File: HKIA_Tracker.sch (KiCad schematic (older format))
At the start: 34 parts

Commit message: sch done
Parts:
- added C? (x5): 10uF, Capacitor_SMD:C_0805_2012Metric, symbol Device:C
- added C? (x6): 100nF, Capacitor_SMD:C_0805_2012Metric, symbol Device:C
- added C?: 10pF, Capacitor_SMD:C_0603_1608Metric, symbol Device:C
- added C?: 150pF, Capacitor_SMD:C_0603_1608Metric, symbol Device:C
- added C?: NC, Capacitor_SMD:C_0603_1608Metric, symbol Device:C
- added C?: 100pF, Capacitor_SMD:C_0603_1608Metric, symbol Device:C
- added C?: 1uF, Capacitor_SMD:C_0603_1608Metric, symbol Device:C
- added C?: 220nF, Capacitor_SMD:C_0603_1608Metric, symbol Device:C
- added C?: 4.7uF, Capacitor_SMD:C_0603_1608Metric, symbol Device:C
- added J?: SWD, Connector_PinHeader_1.27mm:PinHeader_2x05_P1.27mm_Vertical_SMD, symbol Connector_Generic:Conn_02x05_Odd_Even
- added J?: Conn_01x04, symbol Connector_Generic:Conn_01x04
- added L?: 10uH, Inductor_SMD:L_1210_3225Metric, symbol Device:L
- added L?: 22uH, Inductor_SMD:L_1210_3225Metric, symbol Device:L
- added R? (x3): 680k, Resistor_SMD:R_0603_1608Metric, symbol Device:R
- added R? (x3): 120k, Resistor_SMD:R_0603_1608Metric, symbol Device:R
- added R? (x6): 10K, Resistor_SMD:R_0603_1608Metric, symbol Device:R
- added SW? (x3): SW_Push, Button_Switch_SMD:SW_SPST_CK_KXT3, symbol Switch:SW_Push
- added U?: TPS62200DBV, Package_TO_SOT_SMD:SOT-23-5, symbol Regulator_Switching:TPS62200DBV
- added U?: E73-2G4M04S-52832, RF_Module:E73-2G4M04S, symbol RF_Module:E73-2G4M04S-52832
- added U?: ESP-12F, RF_Module:ESP-12E, symbol RF_Module:ESP-12F
- added U?: QMC5883L, Package_LGA:LGA-16_3x3mm_P0.5mm, symbol HKIA_Tracker_SYM:QMC5883L
- C?: value 10n -> 10nF
- C? (x2): value 100n -> 100nF
- R?: value 14K -> 56k; LCSC C103291 -> C304766
- R?: LCSC (none) -> C15402
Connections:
- net labels added: +3.3VP, +BATT, DRDY, ESP_EN, ESP_IO0, ESP_IO2, ESP_RX, ESP_TX, NRF_RX, NRF_TX, SCL, SDA, SWCLK, SWDIO, SWO, nRST
- wire segments 89 -> 216
- no-connect marks 2 -> 5
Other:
- note added: "ANT"
- moved on the sheet: C?, D?, F?, J?, JP?, L?, R?, U?

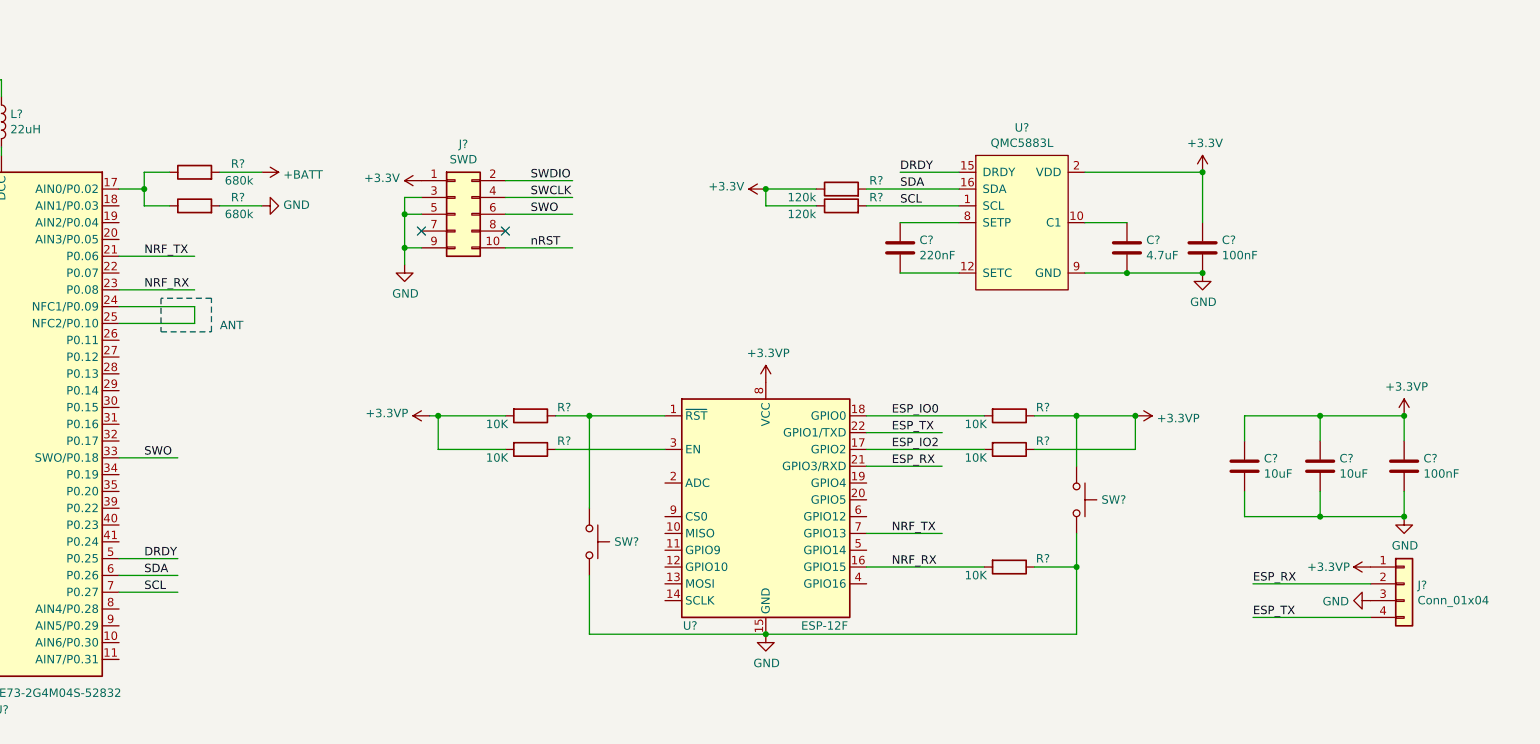
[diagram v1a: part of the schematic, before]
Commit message: add button and led
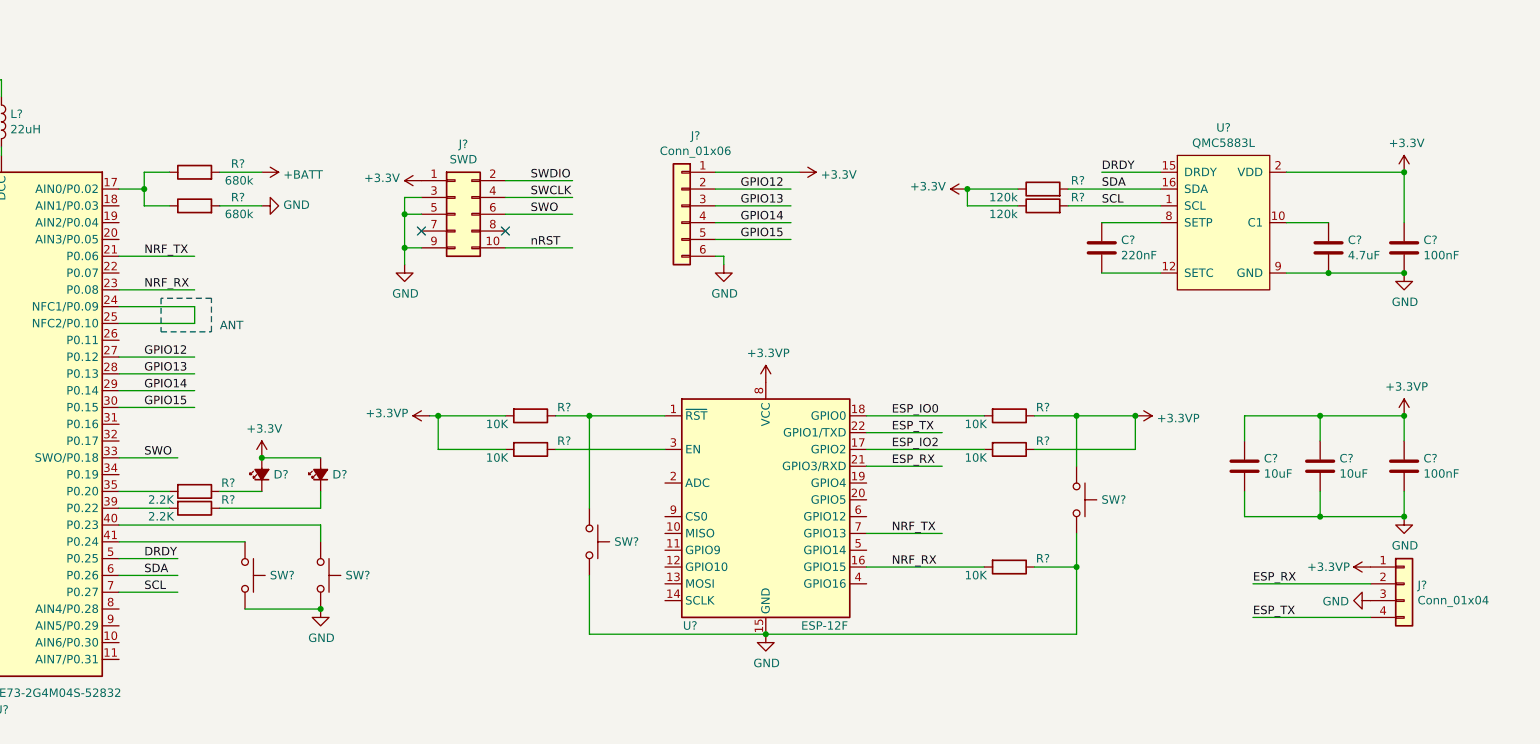
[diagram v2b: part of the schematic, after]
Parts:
- added D? (x2): LED_Small_ALT, Diode_SMD:D_0603_1608Metric, symbol Device:LED_Small_ALT
- added J?: Conn_01x06, Connector_PinHeader_2.54mm:PinHeader_1x06_P2.54mm_Vertical, symbol Connector_Generic:Conn_01x06
- added R? (x2): 2.2K, Resistor_SMD:R_0603_1608Metric, symbol Device:R
- added SW? (x2): SW_Push, Button_Switch_SMD:SW_SPST_CK_KXT3, symbol Switch:SW_Push
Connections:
- net labels added: GPIO12, GPIO13, GPIO14, GPIO15
- wire segments 216 -> 237
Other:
- moved on the sheet: C?, R?, U?

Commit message: fix issues
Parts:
- removed U?: QMC5883L, Package_LGA:LGA-16_3x3mm_P0.5mm, symbol HKIA_Tracker_SYM:QMC5883L
- added U5: QMC5883L, Package_LGA:LGA-16_3x3mm_P0.5mm, symbol HKIA_Tracker_SYM:QMC5883L
- gave numbers to parts that had none: 81
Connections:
- wire segments 237 -> 241
- no-connect marks 5 -> 28
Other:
- moved on the sheet: J4

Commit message: added power jumpers
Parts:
- removed JP1: Jumper_2_Bridged, symbol Jumper:Jumper_2_Bridged
- added JP? (x3): Jumper_NO_Small, Jumper:SolderJumper-2_P1.3mm_Open_RoundedPad1.0x1.5mm, symbol Device:Jumper_NO_Small
- added R29: 0R, Resistor_SMD:R_0603_1608Metric, symbol Device:R
- C10, C11, C15, C23, C24, C25, C5, C6: footprint Capacitor_SMD:C_0805_2012Metric -> Capacitor_SMD:C_0603_1608Metric
- J5: footprint (none) -> Connector_PinHeader_2.54mm:PinHeader_1x04_P2.54mm_Vertical
- R14: footprint (none) -> Resistor_SMD:R_0603_1608Metric
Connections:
- wire segments 241 -> 245
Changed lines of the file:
@@
 F 0 "R14" V 5550 2000 50  0000 C CNN
 F 1 "56k" V 5650 1600 50  0000 C CNN
-F 2 "" V 5530 1800 50  0001 C CNN
+F 2 "Resistor_SMD:R_0603_1608Metric" V 5530 1800 50  0001 C CNN
 F 3 "~" H 5600 1800 50  0001 C CNN
 F 4 "C304766" V 5600 1800 50  0001 C CNN "LCSC"
@@
 Text Label 5900 1900 0    50   ~ 0
 DIS_SW
-$Comp
-L Jumper:Jumper_2_Bridged JP1
-U 1 1 60A9B495
-P 5600 2100
-F 0 "JP1" H 5750 2150 50  0000 C CNN
-F 1 "Jumper_2_Bridged" H 5600 2204 50  0001 C CNN
-F 2 "" H 5600 2100 50  0001 C CNN
-F 3 "~" H 5600 2100 50  0001 C CNN
-	1    5600 2100
-	1    0    0    -1
-$EndComp
-Wire Wire Line
-	5400 2100 5250 2100
 Wire Wire Line
 	5250 2100 5250 1900
@@
 	5750 1900 6200 1900
 Wire Wire Line
-	5800 2100 6200 2100
-Wire Wire Line
 	5750 2250 6200 2250
 Wire Wire Line
@@
 F 0 "C10" H 7715 2296 50  0000 L CNN
 F 1 "100nF" H 7715 2205 50  0000 L CNN
-F 2 "Capacitor_SMD:C_0805_2012Metric" H 7638 2100 50  0001 C CNN
+F 2 "Capacitor_SMD:C_0603_1608Metric" H 7638 2100 50  0001 C CNN
 F 3 "~" H 7600 2250 50  0001 C CNN
 F 4 "C1591" H 7600 2250 50  0001 C CNN "LCSC"
@@
 $EndComp
 Wire Wire Line
-	7600 2100 8100 2100
+	7600 2100 7900 2100
 Connection ~ 7600 2100
 Wire Wire Line
@@
 F 0 "C11" H 7765 1596 50  0000 L CNN
 F 1 "100nF" H 7765 1505 50  0000 L CNN
-F 2 "Capacitor_SMD:C_0805_2012Metric" H 7688 1400 50  0001 C CNN
+F 2 "Capacitor_SMD:C_0603_1608Metric" H 7688 1400 50  0001 C CNN
 F 3 "~" H 7650 1550 50  0001 C CNN
 F 4 "C1591" H 7650 1550 50  0001 C CNN "LCSC"
@@
 	7400 1400 7650 1400
 Connection ~ 7400 1400
-Connection ~ 8150 1400
 Connection ~ 7650 1400
 Wire Wire Line
 	7650 1400 8150 1400
-Connection ~ 8100 2100
 $Comp
 L Connector_Generic:Conn_01x02 J4
@@
 	0    1    1    0
 $EndComp
-Wire Wire Line
-	7400 1200 9100 1200
 NoConn ~ 7400 1700
 NoConn ~ 7400 1900
@@
 	1    0    0    -1
 $EndComp
-Wire Wire Line
-	8100 2100 8550 2100
 $Comp
 L Device:C C14
@@
 F 0 "C15" H 9165 2296 50  0000 L CNN
 F 1 "100nF" H 9165 2205 50  0000 L CNN
-F 2 "Capacitor_SMD:C_0805_2012Metric" H 9088 2100 50  0001 C CNN
+F 2 "Capacitor_SMD:C_0603_1608Metric" H 9088 2100 50  0001 C CNN
 F 3 "~" H 9050 2250 50  0001 C CNN
 F 4 "C1591" H 9050 2250 50  0001 C CNN "LCSC"
@@
 	9500 2300 9850 2300
 Connection ~ 9050 2100
-Wire Wire Line
-	9050 2100 9850 2100
-Connection ~ 8550 2100
 Wire Wire Line
 	8550 2100 9050 2100
@@
 F 0 "C25" H 12665 2446 50  0000 L CNN
 F 1 "100nF" H 12665 2355 50  0000 L CNN
-F 2 "Capacitor_SMD:C_0805_2012Metric" H 12588 2250 50  0001 C CNN
+F 2 "Capacitor_SMD:C_0603_1608Metric" H 12588 2250 50  0001 C CNN
 F 3 "~" H 12550 2400 50  0001 C CNN
 F 4 "C1591" H 12550 2400 50  0001 C CNN "LCSC"
@@
 	10950 2100 11150 2100
 Connection ~ 11150 2100
-$Comp
-L power:+3.3VP #PWR0110
-U 1 1 60BCCFE2
-P 12550 2100
-F 0 "#PWR0110" H 12700 2050 50  0001 C CNN
-F 1 "+3.3VP" H 12565 2273 50  0000 C CNN
-F 2 "" H 12550 2100 50  0001 C CNN
-F 3 "" H 12550 2100 50  0001 C CNN
-	1    12550 2100
-	1    0    0    -1
-$EndComp
 NoConn ~ 6900 1000
 $Comp
@@
 F 0 "C5" H 2565 4696 50  0000 L CNN
 F 1 "100nF" H 2565 4605 50  0000 L CNN
-F 2 "Capacitor_SMD:C_0805_2012Metric" H 2488 4500 50  0001 C CNN
+F 2 "Capacitor_SMD:C_0603_1608Metric" H 2488 4500 50  0001 C CNN
 F 3 "~" H 2450 4650 50  0001 C CNN
 F 4 "C1591" H 2450 4650 50  0001 C CNN "LCSC"
@@
 F 0 "C6" H 2565 5696 50  0000 L CNN
 F 1 "100nF" H 2565 5605 50  0000 L CNN
-F 2 "Capacitor_SMD:C_0805_2012Metric" H 2488 5500 50  0001 C CNN
+F 2 "Capacitor_SMD:C_0603_1608Metric" H 2488 5500 50  0001 C CNN
 F 3 "~" H 2450 5650 50  0001 C CNN
 F 4 "C1591" H 2450 5650 50  0001 C CNN "LCSC"
@@
 F 0 "J5" H 12280 6942 50  0000 L CNN
 F 1 "Conn_01x04" H 12280 6851 50  0000 L CNN
-F 2 "" H 12200 6950 50  0001 C CNN
+F 2 "Connector_PinHeader_2.54mm:PinHeader_1x04_P2.54mm_Vertical" H 12200 6950 50  0001 C CNN
 F 3 "~" H 12200 6950 50  0001 C CNN
 	1    12200 6950
@@
 F 0 "C24" H 12315 6296 50  0000 L CNN
 F 1 "100nF" H 12315 6205 50  0000 L CNN
-F 2 "Capacitor_SMD:C_0805_2012Metric" H 12238 6100 50  0001 C CNN
+F 2 "Capacitor_SMD:C_0603_1608Metric" H 12238 6100 50  0001 C CNN
 F 3 "~" H 12200 6250 50  0001 C CNN
 F 4 "C1591" H 12200 6250 50  0001 C CNN "LCSC"
@@
 	1    0    0    -1
 $EndComp
-Connection ~ 9100 1200
 $Comp
 L power:+BATT #PWR0129
@@
 F 0 "C23" H 12315 4996 50  0000 L CNN
 F 1 "100nF" H 12315 4905 50  0000 L CNN
-F 2 "Capacitor_SMD:C_0805_2012Metric" H 12238 4800 50  0001 C CNN
+F 2 "Capacitor_SMD:C_0603_1608Metric" H 12238 4800 50  0001 C CNN
 F 3 "~" H 12200 4950 50  0001 C CNN
 F 4 "C1591" H 12200 4950 50  0001 C CNN "LCSC"
@@
 NoConn ~ 9000 6450
 NoConn ~ 9000 6350
-$Comp
-L power:PWR_FLAG #FLG0101
-U 1 1 61643EB5
-P 12550 2100
-F 0 "#FLG0101" H 12550 2175 50  0001 C CNN
-F 1 "PWR_FLAG" V 12550 2228 50  0001 L CNN
-F 2 "" H 12550 2100 50  0001 C CNN
-F 3 "~" H 12550 2100 50  0001 C CNN
-	1    12550 2100
-	0    1    1    0
-$EndComp
 Wire Wire Line
 	9000 1300 9050 1300
@@
 $EndComp
 Connection ~ 4350 850
-Wire Wire Line
-	8150 1400 8550 1400
 $Comp
 L power:+3.3V #PWR0106
@@
 L power:VBUS #PWR0138
 U 1 1 616AECAA
-P 9050 2100
-F 0 "#PWR0138" H 9050 1950 50  0001 C CNN
-F 1 "VBUS" H 9065 2273 50  0000 C CNN
-F 2 "" H 9050 2100 50  0001 C CNN
-F 3 "" H 9050 2100 50  0001 C CNN
-	1    9050 2100
+P 7900 2100
+F 0 "#PWR0138" H 7900 1950 50  0001 C CNN
+F 1 "VBUS" H 7915 2273 50  0000 C CNN
+F 2 "" H 7900 2100 50  0001 C CNN
+F 3 "" H 7900 2100 50  0001 C CNN
+	1    7900 2100
 	1    0    0    -1
 $EndComp
@@
 	1    0    0    -1
 $EndComp
+$Comp
+L Device:R R29
+U 1 1 616E726F
+P 5600 2100
+F 0 "R29" V 5550 2300 50  0000 C CNN
+F 1 "0R" V 5650 1900 50  0000 C CNN
+F 2 "Resistor_SMD:R_0603_1608Metric" V 5530 2100 50  0001 C CNN
+F 3 "~" H 5600 2100 50  0001 C CNN
+F 4 "C15402" V 5600 2100 50  0001 C CNN "LCSC"
+	1    5600 2100
+	0    1    1    0
+$EndComp
+Wire Wire Line
+	5750 2100 6200 2100
+Wire Wire Line
+	5250 2100 5450 2100
+Connection ~ 9100 1200
+$Comp
+L Device:Jumper_NO_Small JP?
+U 1 1 617431F3
+P 8350 1200
+F 0 "JP?" H 8350 1293 50  0000 C CNN
+F 1 "Jumper_NO_Small" H 8350 1294 50  0001 C CNN
+F 2 "Jumper:SolderJumper-2_P1.3mm_Open_RoundedPad1.0x1.5mm" H 8350 1200 50  0001 C CNN
+F 3 "~" H 8350 1200 50  0001 C CNN
+	1    8350 1200
+	1    0    0    -1
+$EndComp
+Wire Wire Line
+	7400 1200 8250 1200
+Wire Wire Line
+	8450 1200 9100 1200
+$Comp
+L power:PWR_FLAG #FLG0101
+U 1 1 61643EB5
+P 12550 2100
+F 0 "#FLG0101" H 12550 2175 50  0001 C CNN
+F 1 "PWR_FLAG" V 12550 2228 50  0001 L CNN
+F 2 "" H 12550 2100 50  0001 C CNN
+F 3 "~" H 12550 2100 50  0001 C CNN
+	1    12550 2100
+	0    1    1    0
+$EndComp
+$Comp
+L power:+3.3VP #PWR0110
+U 1 1 60BCCFE2
+P 12550 2100
+F 0 "#PWR0110" H 12700 2050 50  0001 C CNN
+F 1 "+3.3VP" H 12565 2273 50  0000 C CNN
+F 2 "" H 12550 2100 50  0001 C CNN
+F 3 "" H 12550 2100 50  0001 C CNN
+	1    12550 2100
+	1    0    0    -1
+$EndComp
+$Comp
+L Device:Jumper_NO_Small JP?
+U 1 1 6178C491
+P 8350 2100
+F 0 "JP?" H 8350 2193 50  0000 C CNN
+F 1 "Jumper_NO_Small" H 8350 2194 50  0001 C CNN
+F 2 "Jumper:SolderJumper-2_P1.3mm_Open_RoundedPad1.0x1.5mm" H 8350 2100 50  0001 C CNN
+F 3 "~" H 8350 2100 50  0001 C CNN
+	1    8350 2100
+	1    0    0    -1
+$EndComp
+$Comp
+L Device:Jumper_NO_Small JP?
+U 1 1 617BEE0A
+P 8350 1400
+F 0 "JP?" H 8350 1493 50  0000 C CNN
+F 1 "Jumper_NO_Small" H 8350 1494 50  0001 C CNN
+F 2 "Jumper:SolderJumper-2_P1.3mm_Open_RoundedPad1.0x1.5mm" H 8350 1400 50  0001 C CNN
+F 3 "~" H 8350 1400 50  0001 C CNN
+	1    8350 1400
+	1    0    0    -1
+$EndComp
+Wire Wire Line
+	8150 1400 8250 1400
+Connection ~ 8150 1400
+Wire Wire Line
+	8450 1400 8550 1400
+Connection ~ 7900 2100
+Wire Wire Line
+	7900 2100 8100 2100
+Wire Wire Line
+	8100 2100 8250 2100
+Connection ~ 8100 2100
+Wire Wire Line
+	8450 2100 8550 2100
+Connection ~ 8550 2100
+Wire Wire Line
+	9050 2100 9850 2100
 $EndSCHEMATC

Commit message: save
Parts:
- gave numbers to parts that had none: 3
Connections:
- wire segments 245 -> 247
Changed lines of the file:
@@
 L power:+BATT #PWR0128
 U 1 1 6115DFF2
-P 9100 1200
-F 0 "#PWR0128" H 9100 1050 50  0001 C CNN
-F 1 "+BATT" H 9115 1373 50  0000 C CNN
-F 2 "" H 9100 1200 50  0001 C CNN
-F 3 "" H 9100 1200 50  0001 C CNN
-	1    9100 1200
+P 8150 1200
+F 0 "#PWR0128" H 8150 1050 50  0001 C CNN
+F 1 "+BATT" H 8165 1373 50  0000 C CNN
+F 2 "" H 8150 1200 50  0001 C CNN
+F 3 "" H 8150 1200 50  0001 C CNN
+	1    8150 1200
 	1    0    0    -1
 $EndComp
@@
 Wire Wire Line
 	5250 2100 5450 2100
-Connection ~ 9100 1200
-$Comp
-L Device:Jumper_NO_Small JP?
+$Comp
+L Device:Jumper_NO_Small JP1
 U 1 1 617431F3
 P 8350 1200
-F 0 "JP?" H 8350 1293 50  0000 C CNN
+F 0 "JP1" H 8350 1293 50  0000 C CNN
 F 1 "Jumper_NO_Small" H 8350 1294 50  0001 C CNN
 F 2 "Jumper:SolderJumper-2_P1.3mm_Open_RoundedPad1.0x1.5mm" H 8350 1200 50  0001 C CNN
@@
 $EndComp
 Wire Wire Line
-	7400 1200 8250 1200
+	7400 1200 8150 1200
 Wire Wire Line
 	8450 1200 9100 1200
@@
 $EndComp
 $Comp
-L Device:Jumper_NO_Small JP?
+L Device:Jumper_NO_Small JP3
 U 1 1 6178C491
 P 8350 2100
-F 0 "JP?" H 8350 2193 50  0000 C CNN
+F 0 "JP3" H 8350 2193 50  0000 C CNN
 F 1 "Jumper_NO_Small" H 8350 2194 50  0001 C CNN
 F 2 "Jumper:SolderJumper-2_P1.3mm_Open_RoundedPad1.0x1.5mm" H 8350 2100 50  0001 C CNN
@@
 $EndComp
 $Comp
-L Device:Jumper_NO_Small JP?
+L Device:Jumper_NO_Small JP2
 U 1 1 617BEE0A
 P 8350 1400
-F 0 "JP?" H 8350 1493 50  0000 C CNN
+F 0 "JP2" H 8350 1493 50  0000 C CNN
 F 1 "Jumper_NO_Small" H 8350 1494 50  0001 C CNN
 F 2 "Jumper:SolderJumper-2_P1.3mm_Open_RoundedPad1.0x1.5mm" H 8350 1400 50  0001 C CNN
@@
 Connection ~ 8150 1400
 Wire Wire Line
-	8450 1400 8550 1400
+	8450 1400 8500 1400
 Connection ~ 7900 2100
 Wire Wire Line
@@
 Wire Wire Line
 	9050 2100 9850 2100
+Connection ~ 8150 1200
+Wire Wire Line
+	8150 1200 8250 1200
+$Comp
+L power:PWR_FLAG #FLG0105
+U 1 1 6183C64B
+P 8550 2100
+F 0 "#FLG0105" H 8550 2175 50  0001 C CNN
+F 1 "PWR_FLAG" H 8550 2273 50  0001 C CNN
+F 2 "" H 8550 2100 50  0001 C CNN
+F 3 "~" H 8550 2100 50  0001 C CNN
+	1    8550 2100
+	1    0    0    -1
+$EndComp
+$Comp
+L power:PWR_FLAG #FLG0106
+U 1 1 6183CADD
+P 8500 1400
+F 0 "#FLG0106" H 8500 1475 50  0001 C CNN
+F 1 "PWR_FLAG" H 8500 1573 50  0001 C CNN
+F 2 "" H 8500 1400 50  0001 C CNN
+F 3 "~" H 8500 1400 50  0001 C CNN
+	1    8500 1400
+	1    0    0    -1
+$EndComp
+Connection ~ 8500 1400
+Wire Wire Line
+	8500 1400 8550 1400
 $EndSCHEMATC
